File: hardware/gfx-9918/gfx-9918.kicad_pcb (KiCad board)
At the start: 2 copper layers, 25 parts, among them J1 GFX_Connector_Input, J2 CVBS Out, U1 TMS9918, U2 74HCT04, U3 74HCT574, U4 74HCT574, U5 74HCT574, U6 HM62256ALP-10, U7 74HC32, Y1 10.7386Mhz

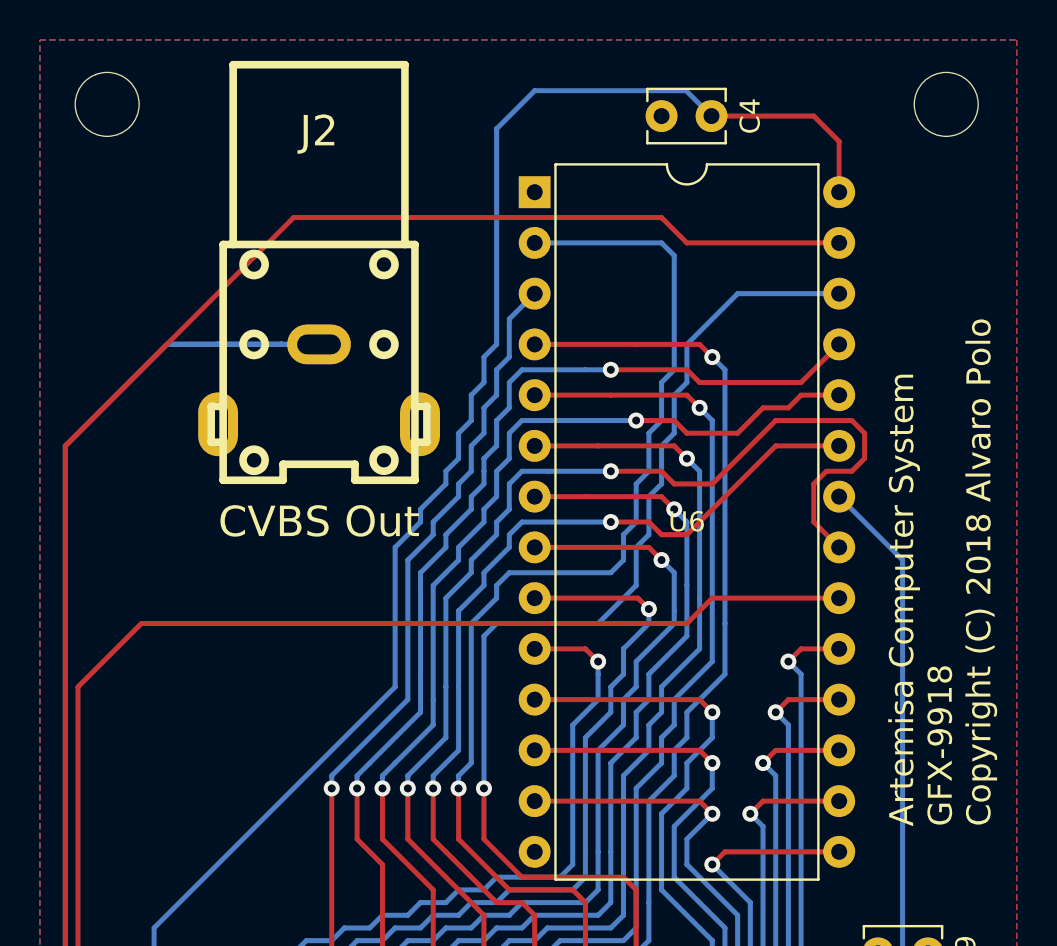
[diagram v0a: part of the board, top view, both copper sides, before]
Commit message: Make so aesthetic changes to GFX-9918
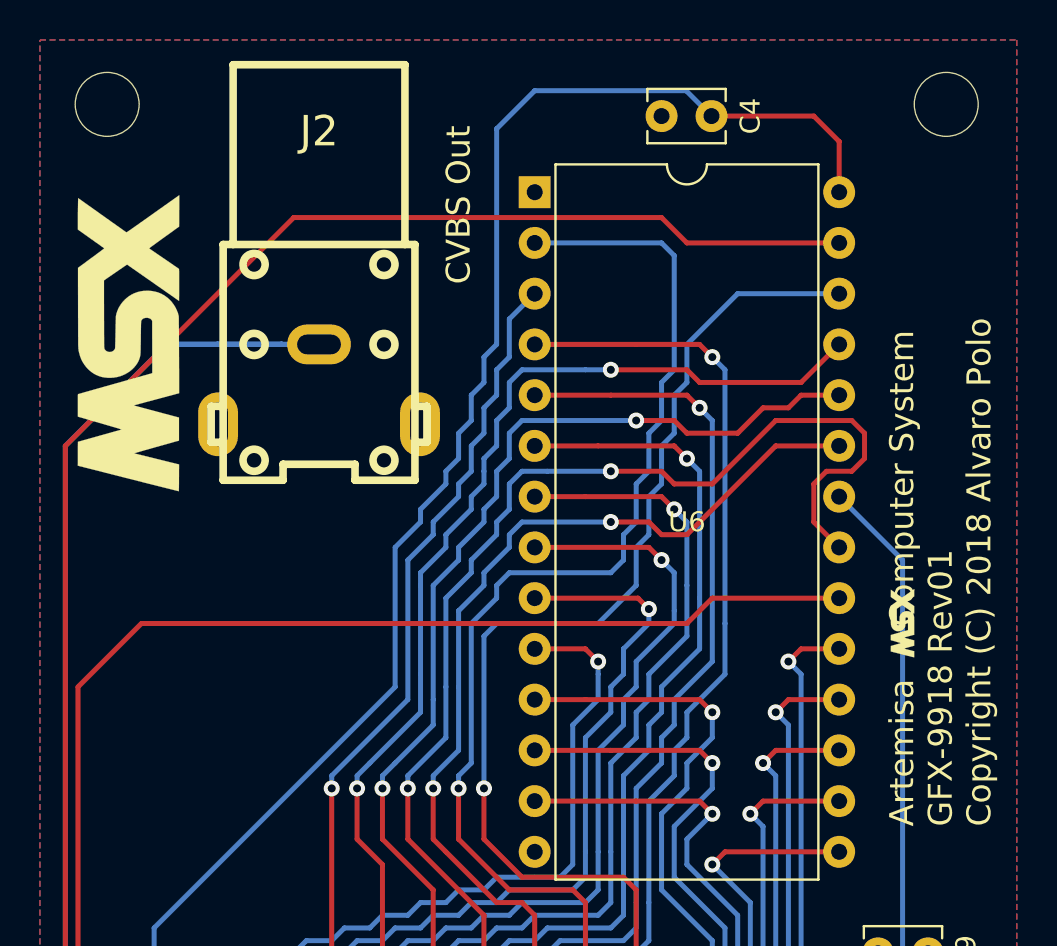
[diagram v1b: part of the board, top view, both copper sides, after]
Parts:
- added G***: LOGO, artemsx:MSX_logo, F.Cu at (49.1, 54.0)
- added G***: LOGO, artemsx:MSX_logo_small, F.Cu at (87.8, 68.0)
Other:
- board text added: "Artemisa Computer System GFX-9918 Rev01 Copyright (C) 2018 Alvaro Polo"
- board text removed: "Artemisa Computer System GFX-9918 Copyright (C) 2018 Alvaro Polo"

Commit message: Remove traces of ArteMSX in hardware files
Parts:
- C1, C2, C3, C4, C5, C6, C7, C8, C9: footprint artemsx:Disc_capacitor -> artemisa:Disc_capacitor
- C11: footprint artemsx:Radial_capacitor -> artemisa:Radial_capacitor
- G***: footprint artemsx:MSX_logo -> artemisa:MSX_logo
- G***: footprint artemsx:MSX_logo_small -> artemisa:MSX_logo_small
- J1: footprint artemsx:GFX_conn -> artemisa:GFX_conn
- J2: footprint artemsx:RCA -> artemisa:RCA
- R1: footprint artemsx:Axial_resistor -> artemisa:Axial_resistor
- REF** (x4): footprint artemsx:Mounting_hole_M3 -> artemisa:Mounting_hole_M3
- U1: footprint artemsx:DIP-40_600 -> artemisa:DIP-40_600
- U2, U7: footprint artemsx:DIP-14_300 -> artemisa:DIP-14_300
- U3, U4, U5: footprint artemsx:DIP-20_300 -> artemisa:DIP-20_300
- U6: footprint artemsx:DIP-28_600 -> artemisa:DIP-28_600
- Y1: footprint artemsx:Crystal -> artemisa:Crystal

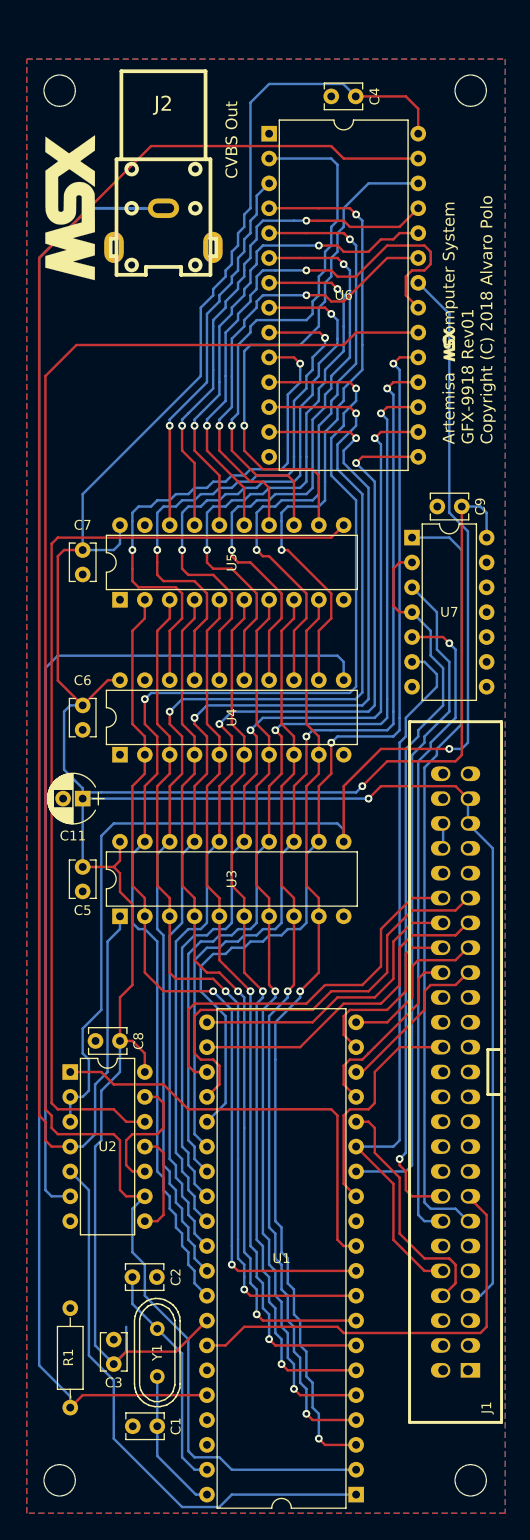
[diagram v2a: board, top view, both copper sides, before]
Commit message: Take `SOUNDOUT` from GFX input in PCB
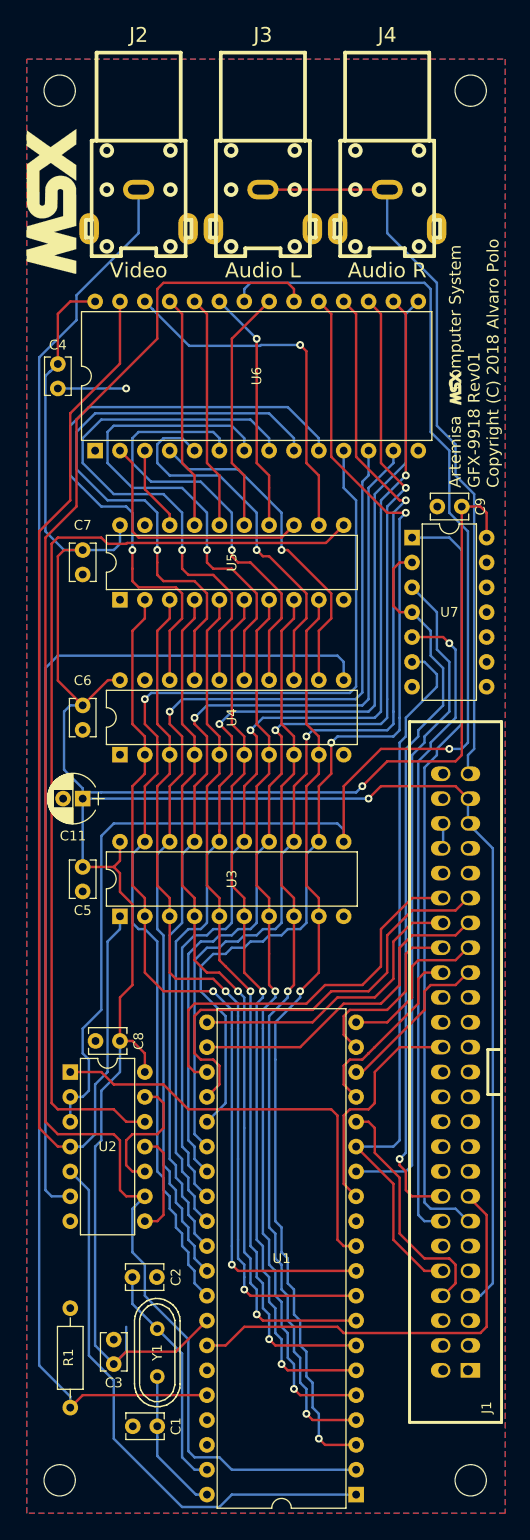
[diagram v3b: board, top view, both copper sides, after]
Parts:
- added J3: Audio L, artemisa:RCA_white, F.Cu at (68.8, 52.1)
- added J4: Audio R, artemisa:RCA_red, F.Cu at (81.5, 52.1)
- J2: value CVBS Out -> Video; footprint artemisa:RCA -> artemisa:RCA_yellow
- moved C4 40.9 mm to (47.8, 69.9), turned to 270 degrees
- moved U6 36.9 mm to (51.6, 78.8), turned to 90 degrees
- moved G*** 4.49 mm to (88.5, 72.4)
- moved J2 3.18 mm to (56.1, 52.1)
- moved G*** 2.01 mm to (47.2, 53.4)
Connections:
- J1 pad 49: Net-(J1-Pad49) -> /SOUNDOUT
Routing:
- net /SOUNDOUT: track 0.00 -> 76.3 mm
- net /RD: track 163.6 -> 118.2 mm
- net VCC: track 369.2 -> 326.5 mm
- net Net-(U5-Pad15): track 57.0 -> 25.0 mm, vias 2 -> 0
- net Net-(U4-Pad12): track 65.3 -> 34.2 mm, vias 2 -> 1
- net Net-(U5-Pad18): track 39.1 -> 8.67 mm, vias 1 -> 0
- net Net-(U5-Pad13): track 56.0 -> 26.1 mm, vias 1 -> 0
- net Net-(U5-Pad17): track 52.0 -> 23.9 mm, vias 2 -> 0
- net Net-(U5-Pad16): track 49.4 -> 23.9 mm, vias 2 -> 0
- net Net-(U4-Pad13): track 63.6 -> 38.9 mm, vias 2 -> 1
- net Net-(U5-Pad14): track 46.2 -> 25.0 mm, vias 2 -> 1
- net /WR: track 127.9 -> 147.6 mm
- net Net-(U5-Pad12): track 54.4 -> 37.0 mm
- net /VD0: track 129.9 -> 112.8 mm, vias 2 -> 1
- net Net-(U4-Pad14): track 62.4 -> 46.0 mm, vias 2 -> 1
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
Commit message: Fix power pin arrangement in GFX9918
For discrete logic symbols, add a new one to represent the power connections. So we can represent them in the schematic explicitely. 

This also fixes the different format in capacitor values.
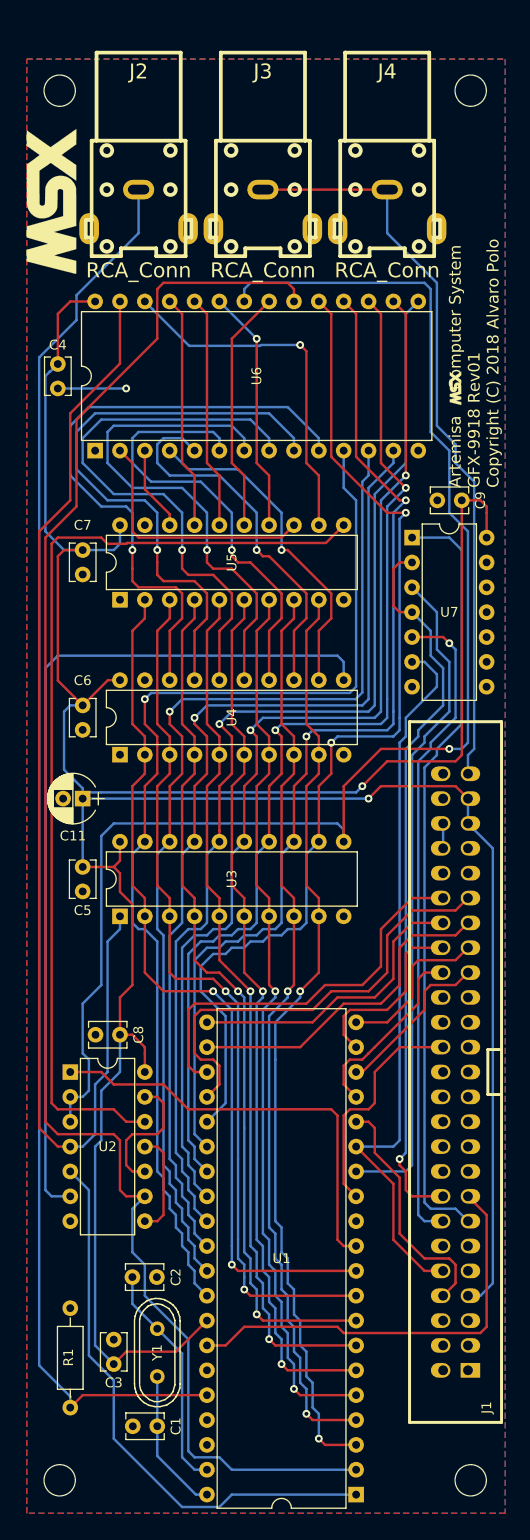
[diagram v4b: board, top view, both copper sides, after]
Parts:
- C5, C6, C7, C8, C9: value .1uF -> 100nF
- J2: value Video -> RCA_Conn
- J3: value Audio L -> RCA_Conn
- J4: value Audio R -> RCA_Conn
- moved C9 0.64 mm to (89.1, 83.9)
- moved C8 0.63 mm to (54.2, 138.5)
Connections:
- net VCC renamed ~
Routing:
- net ~: track 326.5 -> 324.1 mm

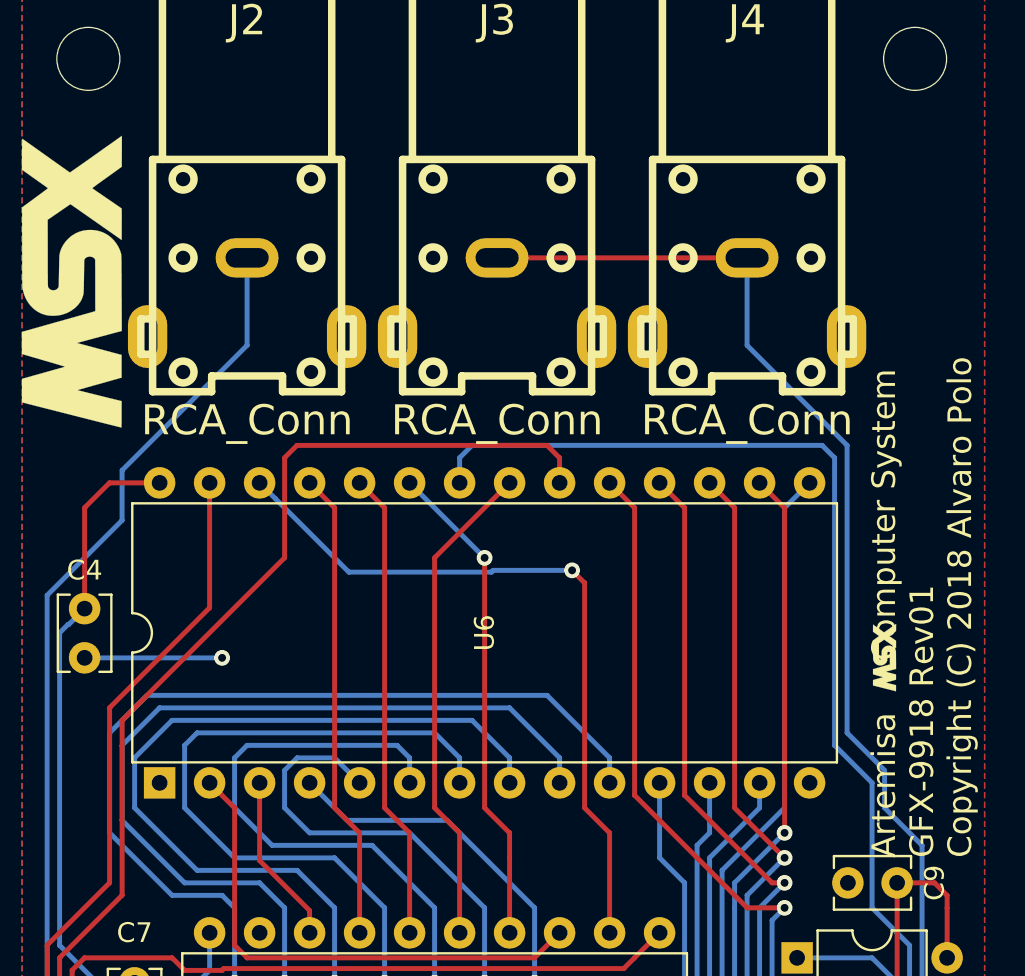
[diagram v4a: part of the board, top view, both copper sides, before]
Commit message: Fix wrong pin layout of RCA connector footprints
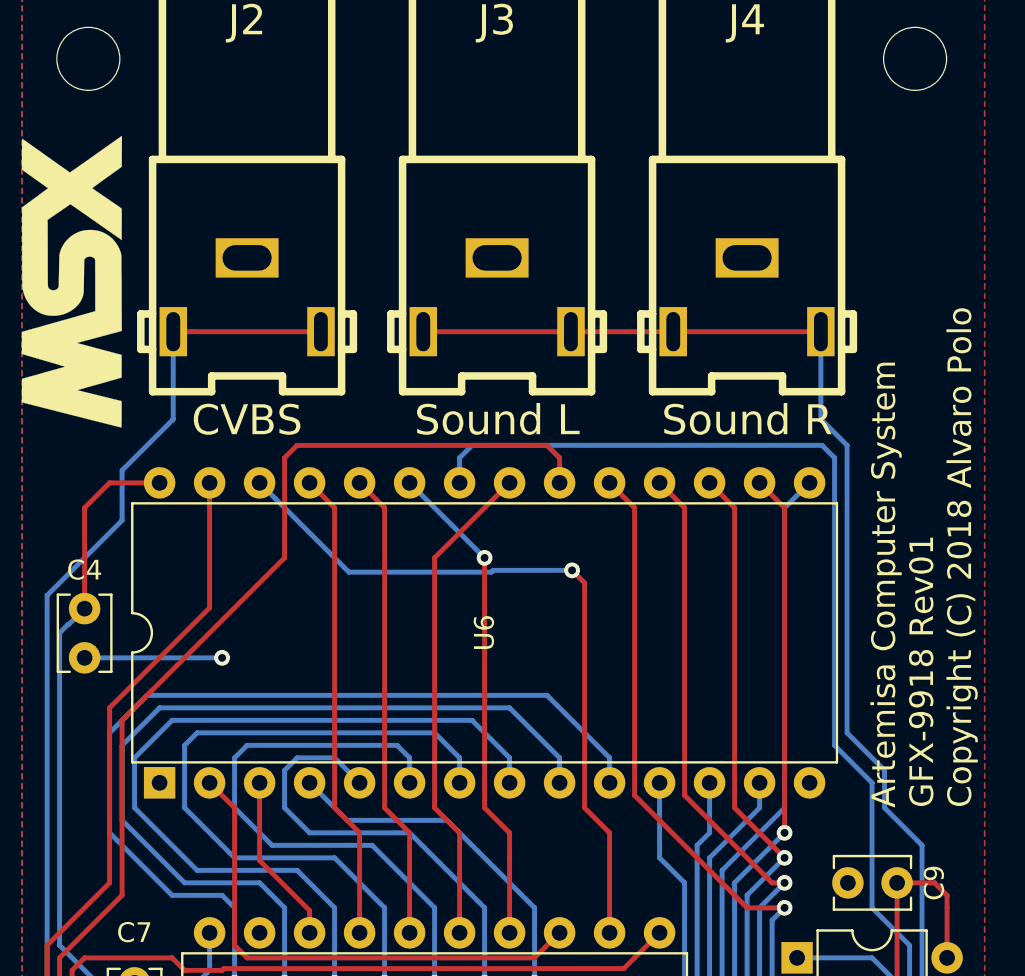
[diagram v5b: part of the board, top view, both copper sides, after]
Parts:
- removed the G*** at (88.5, 72.4)
- J2: value RCA_Conn -> CVBS
- J3: value RCA_Conn -> Sound L
- J4: value RCA_Conn -> Sound R
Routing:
- net Net-(J2-Pad1): track 144.5 -> 146.7 mm
- net /SOUNDOUT: track 76.3 -> 78.5 mm

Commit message: Fix missing footprint 3D models
Even add a custom one for the MSX slot connector.
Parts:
- J2: value CVBS -> AV
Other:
- board outline added: 50 x 150 mm
- board text added: "Artemisa Computer System GFX9918 Rev02 Copyright (C) 2018 Alvaro Polo"
- board text removed: "Artemisa Computer System GFX-9918 Rev01 Copyright (C) 2018 Alvaro Polo"

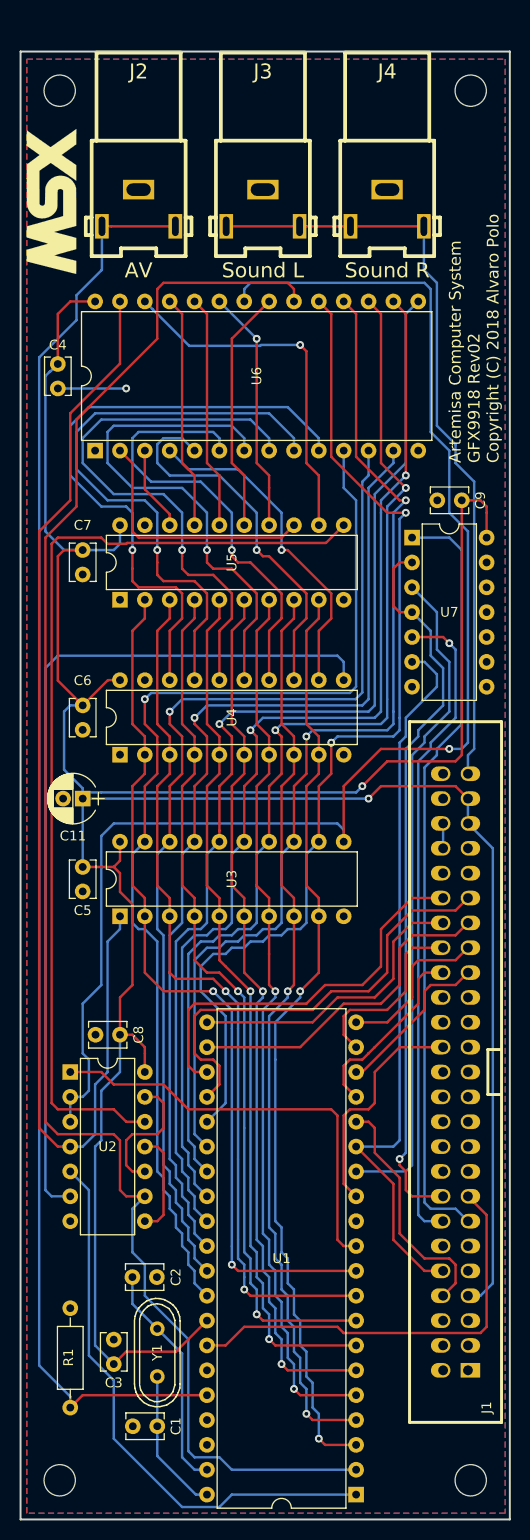
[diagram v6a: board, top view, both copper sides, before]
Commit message: Increase width of power tracks in GFX9918
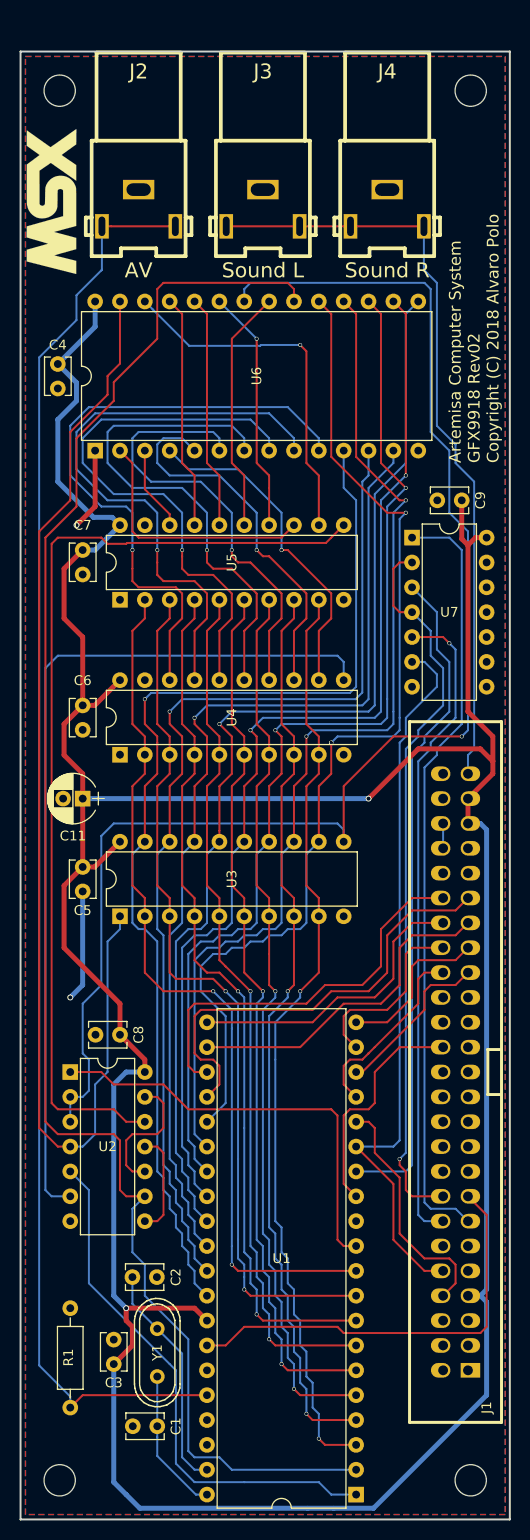
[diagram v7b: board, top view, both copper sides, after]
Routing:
- net ~: track 324.1 -> 347.7 mm
- net GND: track 6.98 -> 19.8 mm, vias 1 -> 2
- net /~RAS: track 57.3 -> 54.0 mm
- net /WR: track 147.6 -> 146.8 mm
- net /VD7: vias 2 -> 3
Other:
- net class Default: clearance 0.2 -> 0.2032; trace_width 0.25 -> 0.2032; via_dia 0.8 -> 0.4064; via_drill 0.4 -> 0.3048
- net class Power added: clearance 0.254, trace_width 0.508, via_dia 0.6096, via_drill 0.4064
- rule trace_clearance: 0.2 -> 0.2032
- rule trace_min: 0.2 -> 0.1524
- rule via_min_drill: 0.3 -> 0.3048
- rule via_min_size: 0.4 -> 0.4064
